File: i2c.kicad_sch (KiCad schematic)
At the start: 15 parts, among them CN8 GPS, J5 IPL1-102-01-X-D-K, U1 BNO055, Y2 8MHz

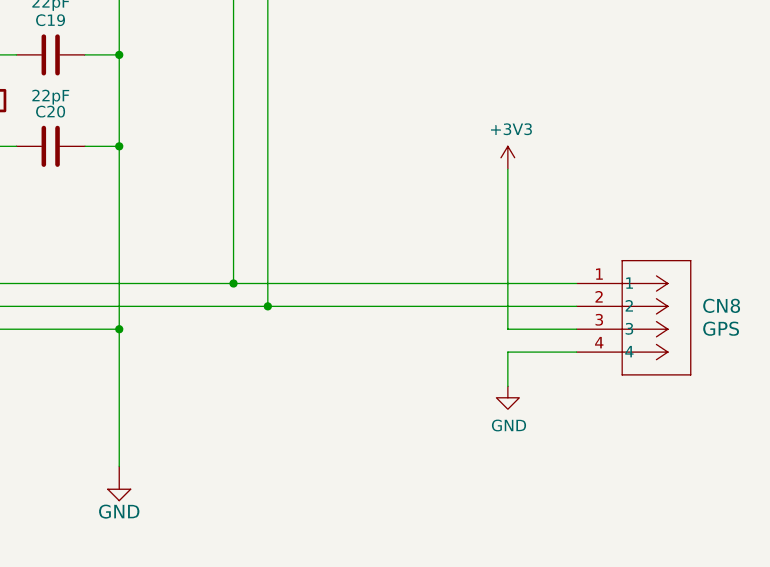
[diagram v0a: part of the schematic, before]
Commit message: All review changes complete, except update CAN connector
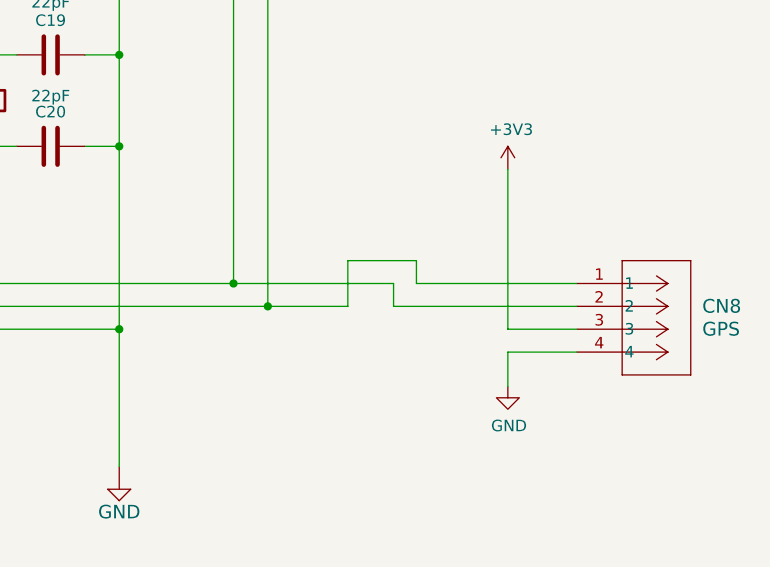
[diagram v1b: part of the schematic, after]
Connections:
- net SCL: now also CN8.1; no longer CN8.2
- net SDA: now also CN8.2; no longer CN8.1
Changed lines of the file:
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@@
+	)
+	(junction
+		(at 207.01 118.11)
+		(diameter 0)
+		(color 0 0 0 0)
 	)
 	(junction
@@
 	)
 	(junction
+		(at 166.37 120.65)
+		(diameter 0)
+		(color 0 0 0 0)
+	)
+	(junction
+		(at 156.21 66.04)
+		(diameter 0)
+		(color 0 0 0 0)
+	)
+	(junction
 		(at 210.82 120.65)
 		(diameter 0)
@@
 	)
 	(junction
-		(at 166.37 120.65)
-		(diameter 0)
-		(color 0 0 0 0)
-	)
-	(junction
-		(at 156.21 66.04)
-		(diameter 0)
-		(color 0 0 0 0)
-	)
-	(junction
 		(at 77.47 76.2)
 		(diameter 0)
@@
 	)
 	(junction
-		(at 207.01 118.11)
-		(diameter 0)
-		(color 0 0 0 0)
-	)
-	(junction
 		(at 194.31 123.19)
 		(diameter 0)
@@
 	(wire
 		(pts
+			(xy 227.33 118.11) (xy 245.11 118.11)
+		)
+		(stroke
+			(width 0)
+			(type default)
+		)
+	)
+	(wire
+		(pts
 			(xy 171.45 100.33) (xy 171.45 92.71)
 		)
@@
 	(wire
 		(pts
+			(xy 224.79 120.65) (xy 245.11 120.65)
+		)
+		(stroke
+			(width 0)
+			(type default)
+		)
+	)
+	(wire
+		(pts
 			(xy 104.14 158.75) (xy 119.38 158.75)
 		)
@@
 	(wire
 		(pts
+			(xy 219.71 115.57) (xy 227.33 115.57)
+		)
+		(stroke
+			(width 0)
+			(type default)
+		)
+	)
+	(wire
+		(pts
 			(xy 156.21 66.04) (xy 156.21 83.82)
 		)
@@
 	(wire
 		(pts
+			(xy 219.71 120.65) (xy 219.71 115.57)
+		)
+		(stroke
+			(width 0)
+			(type default)
+		)
+	)
+	(wire
+		(pts
 			(xy 156.21 118.11) (xy 161.29 118.11)
 		)
@@
 	(wire
 		(pts
+			(xy 207.01 118.11) (xy 224.79 118.11)
+		)
+		(stroke
+			(width 0)
+			(type default)
+		)
+	)
+	(wire
+		(pts
 			(xy 161.29 69.85) (xy 161.29 66.04)
 		)
@@
 	(wire
 		(pts
-			(xy 207.01 118.11) (xy 245.11 118.11)
-		)
-		(stroke
-			(width 0)
-			(type default)
-		)
-	)
-	(wire
-		(pts
 			(xy 57.15 110.49) (xy 90.17 110.49)
 		)
@@
 	(wire
 		(pts
+			(xy 227.33 115.57) (xy 227.33 118.11)
+		)
+		(stroke
+			(width 0)
+			(type default)
+		)
+	)
+	(wire
+		(pts
 			(xy 147.32 158.75) (xy 147.32 162.56)
 		)
@@
 	(wire
 		(pts
+			(xy 224.79 118.11) (xy 224.79 120.65)
+		)
+		(stroke
+			(width 0)
+			(type default)
+		)
+	)
+	(wire
+		(pts
 			(xy 147.32 156.21) (xy 147.32 147.32)
 		)
@@
 	(wire
 		(pts
+			(xy 210.82 120.65) (xy 219.71 120.65)
+		)
+		(stroke
+			(width 0)
+			(type default)
+		)
+	)
+	(wire
+		(pts
 			(xy 194.31 102.87) (xy 194.31 123.19)
 		)
@@
 		)
 		(stroke
-			(width 0)
-			(type default)
-		)
-	)
-	(wire
-		(pts
-			(xy 210.82 120.65) (xy 245.11 120.65)
-		)
-		(stroke

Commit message: more changes
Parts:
- L2: value GREEN -> ORANGE
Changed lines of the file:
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@@
 			)
 		)
-		(property "Value" "GREEN"
+		(property "Value" "ORANGE"
 			(at 61.976 148.6154 90)
 			(effects
